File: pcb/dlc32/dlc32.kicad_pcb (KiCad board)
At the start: 2 copper layers, 99.8 x 43.9 mm, 62 parts, among them IC1 74HCT08, IC2 74HCT14, J1 DOOR1, J10 CHILLER SSR PWR, J11 EXHAUST, J12 EXT1, J13 COM2, J14 DLC32:J18, J15 INT PWR, J16 TP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

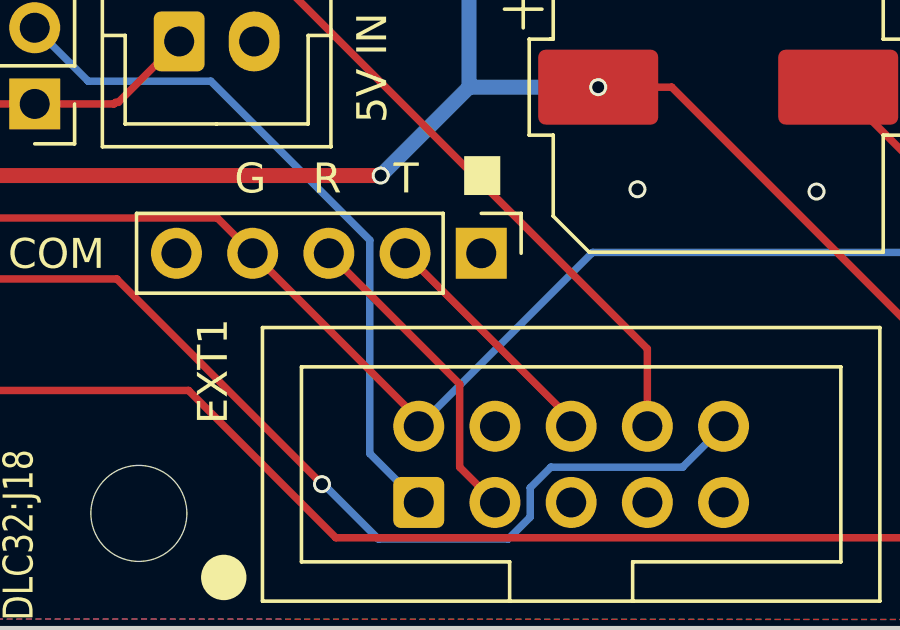
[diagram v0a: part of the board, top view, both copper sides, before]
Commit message: Swap RX and TX.
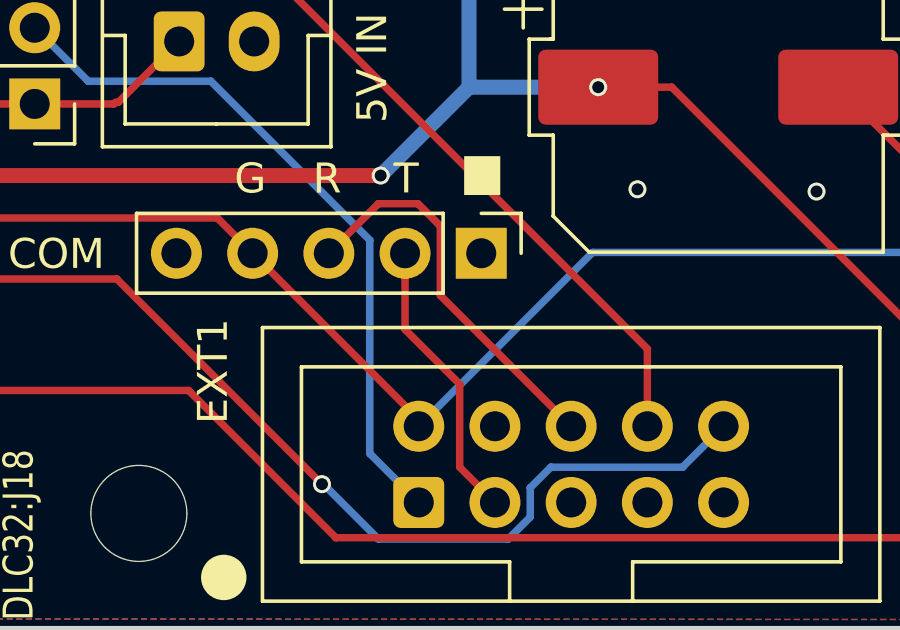
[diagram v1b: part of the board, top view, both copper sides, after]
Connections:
- J13 pad 2: TX -> RX
- J13 pad 3: RX -> TX
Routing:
- net TX: track 8.06 -> 13.4 mm
- net RX: track 10.6 -> 9.55 mm
